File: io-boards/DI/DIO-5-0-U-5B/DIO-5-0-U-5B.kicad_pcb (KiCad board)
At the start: 2 copper layers, 50 x 33 mm, 13 parts, among them J1 GPP_Conn_01x12_Pin, J2 Conn_01x03_Pin, J3 Conn_01x02_Socket, J4 Conn_01x02_Socket, U1 PC817

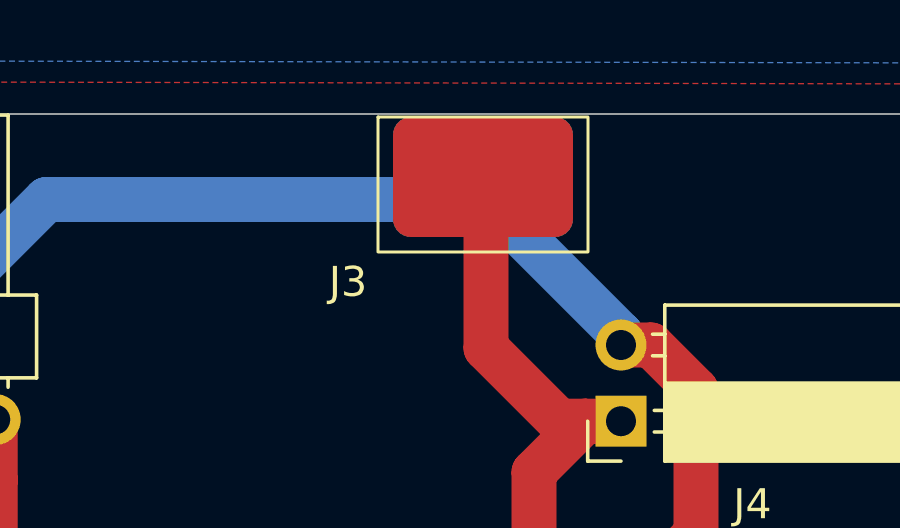
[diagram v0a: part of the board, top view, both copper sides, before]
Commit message: Added Analog Output board for DIP components for testing
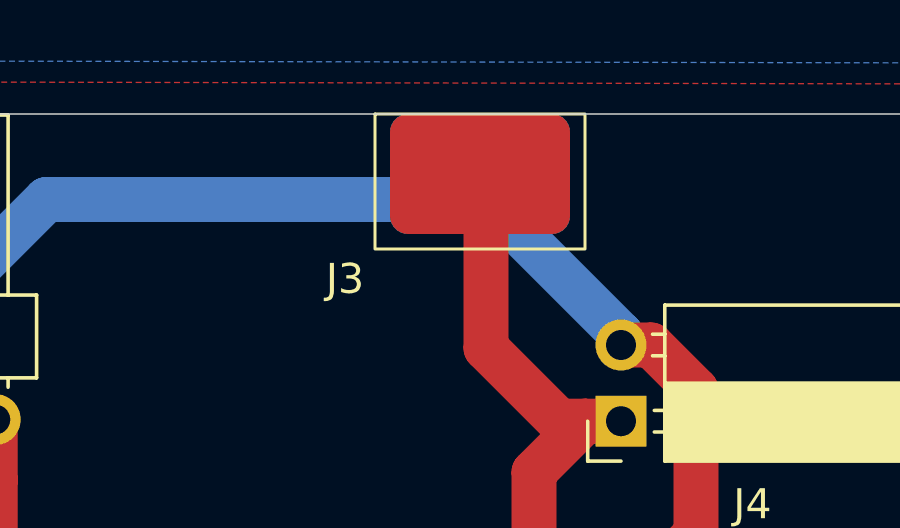
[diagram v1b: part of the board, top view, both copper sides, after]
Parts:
- moved J3 0.14 mm to (135.0, 50.0)
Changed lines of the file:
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@@
 	(footprint "tuxmio:KF141x_SMD"
 		(layer "F.Cu")
-		(at 135.1 50.1)
+		(at 135 50)
 		(property "Reference" "J3"
 			(at -4.5 5.5 0)
